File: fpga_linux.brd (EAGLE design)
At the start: 34 x 31.5 mm, 127 parts, among them IC1 E1109AFGB, IC2 LFE5U-25F68G256CFDG

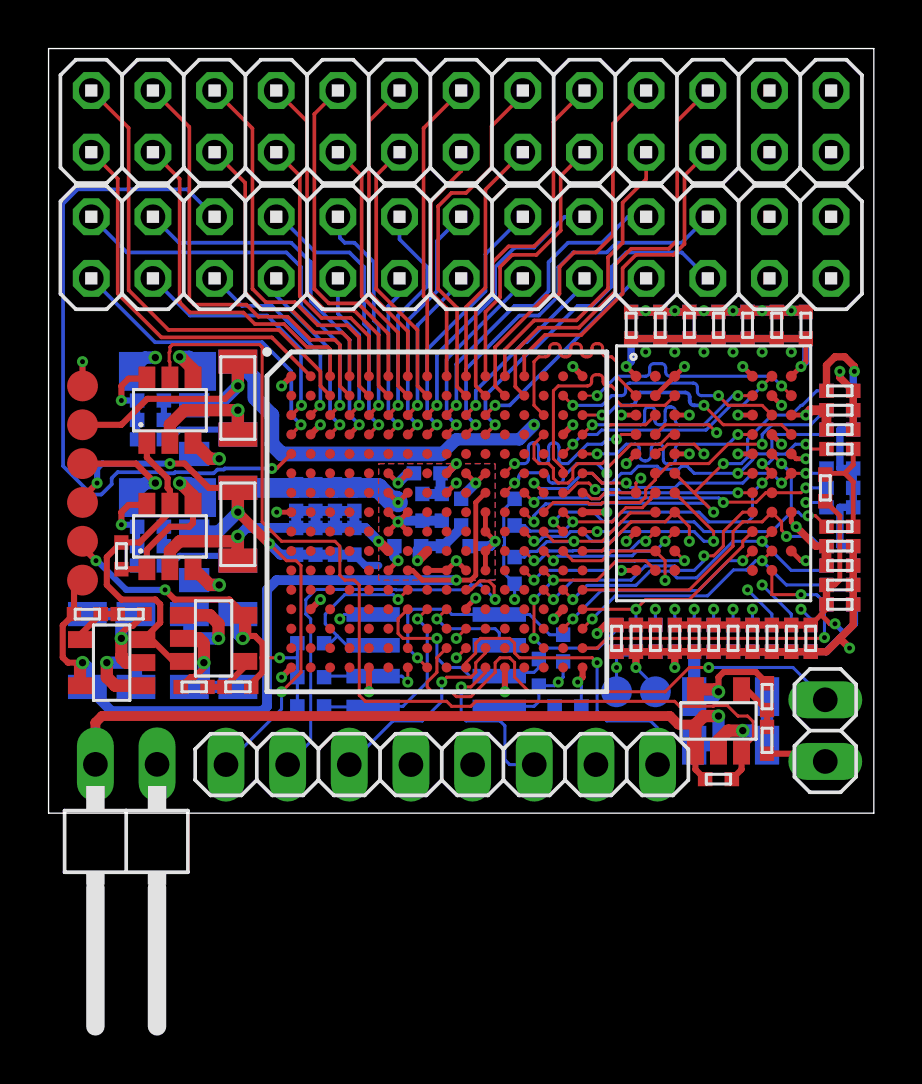
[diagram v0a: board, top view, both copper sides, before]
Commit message: Added gregs recommendations (pullup/down on grogramn/tck, usrled)
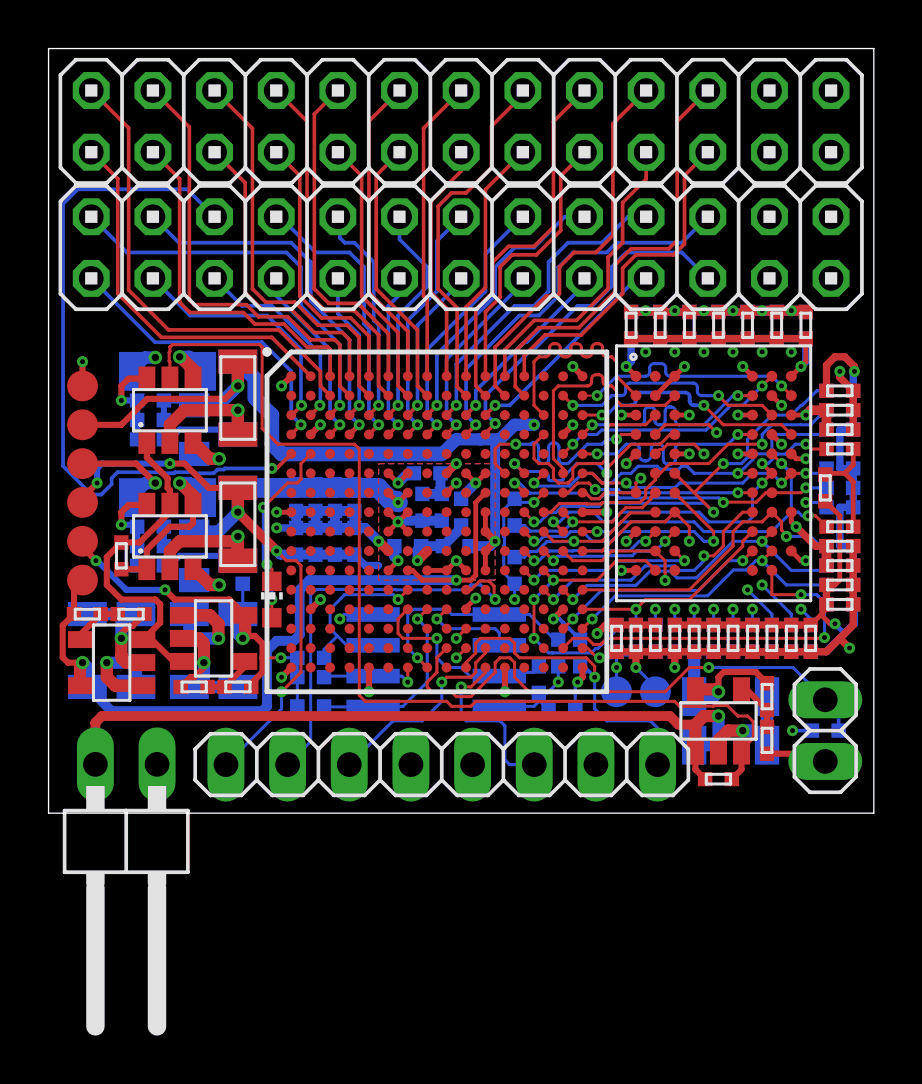
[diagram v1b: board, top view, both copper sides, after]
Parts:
- added LED1: (no value), led:CHIP-LED0603
- added R31, R32, R33: (no value), my_lib:0402
- moved R6 0.60 mm to (17.8, 11.8)
- moved R7 0.30 mm to (27.2, 10.9)
- moved C1 0.29 mm to (28.1, 9.65)
- moved R4 0.28 mm to (28.0, 12.0)
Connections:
- removed net RAM_DU: IC2.F13
- new net LED_N: IC2.E2, LED1.C
- new net N$2: LED1.A, R33.2
- net +3V3: now also R31.2, R33.1
- net GND: now also R32.1
- net RAM_A13: now also IC2.R15; no longer IC2.R16
- net RAM_D3: now also IC2.F13; no longer IC2.G12
- net RAM_RAS_N: now also IC2.F14; no longer IC2.G14
- net RESET_N: now also R31.1
- net TCK: now also R32.2
- net VTT: now also IC2.G14, IC2.R16
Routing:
- net LED_N: track 0.00 -> 6.44 mm, vias 0 -> 2
- net 1V8: track 63.5 -> 68.3 mm
- net VTT: track 67.7 -> 70.9 mm, vias 6 -> 8
- net RESET_N: track 21.3 -> 22.8 mm
- net N$2: track 0.00 -> 1.44 mm, vias 0 -> 1
- net RAM_A13: track 15.0 -> 16.0 mm
- net RAM_CS_N: track 13.2 -> 14.1 mm
- net +3V3: track 31.8 -> 32.7 mm, vias 10 -> 11
- net RAM_D4: track 8.65 -> 9.50 mm
- net TCK: track 13.2 -> 13.8 mm
- net GND: track 119.7 -> 119.6 mm, vias 44 -> 45
